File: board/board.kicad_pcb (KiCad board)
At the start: 2 copper layers, 21 x 13 mm, 10 parts, among them J1 003_power, J2 003_power, U1 TC1017

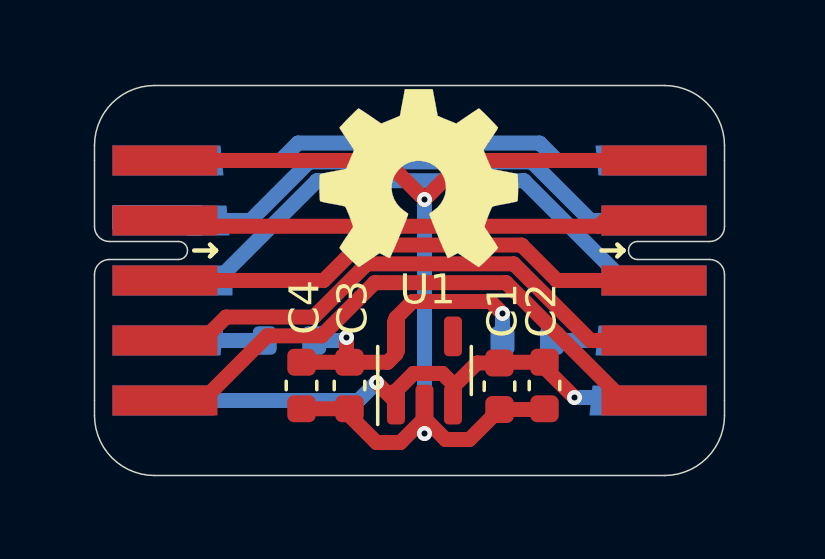
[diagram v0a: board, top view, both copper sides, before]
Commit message: added pours, silkscreen names and updated put_on_edge
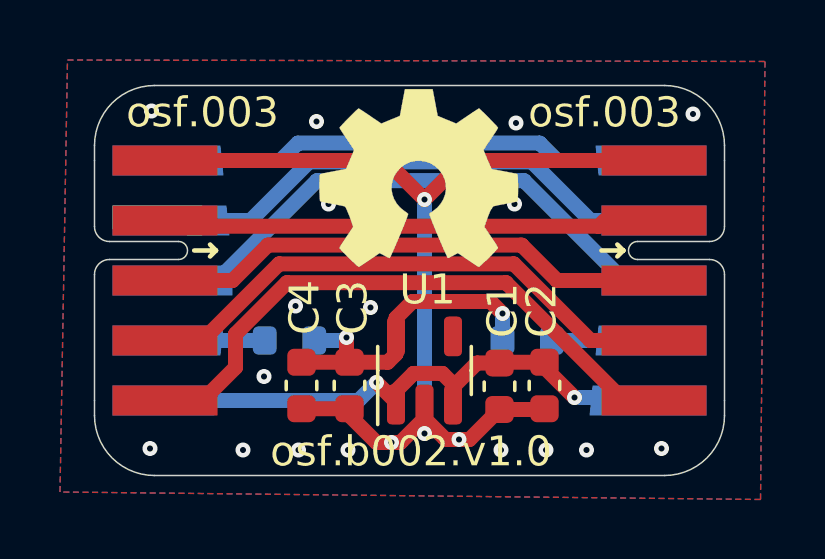
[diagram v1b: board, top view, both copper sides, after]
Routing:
- net Net-(J1-Pad5): track 19.6 -> 20.2 mm
- net /ldo/GND: vias 2 -> 25
- added copper zone on B.Cu, net /ldo/GND
- added copper zone on F.Cu, net /ldo/GND
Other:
- board text added: "osf.003"
- board text added: "osf.b002.v1.0"
